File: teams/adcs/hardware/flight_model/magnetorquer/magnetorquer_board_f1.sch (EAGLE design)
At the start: 35 parts, among them U5 LTC3624

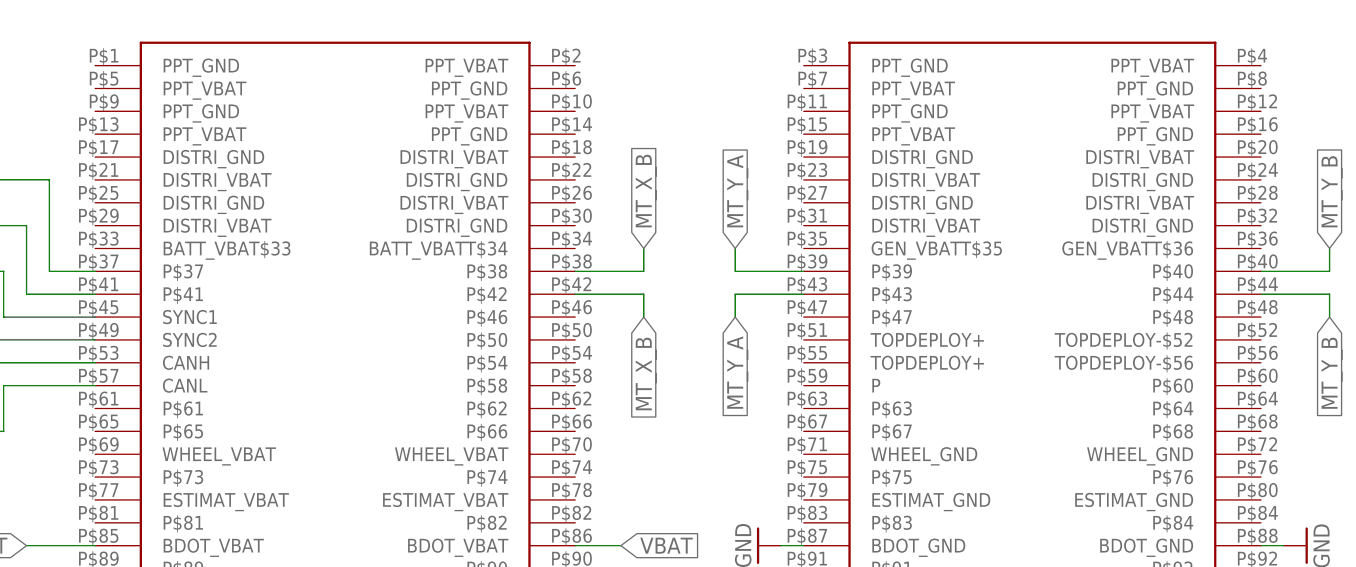
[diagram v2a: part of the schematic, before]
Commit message: ADCS/MT: Move buck converter and clean up stray traces
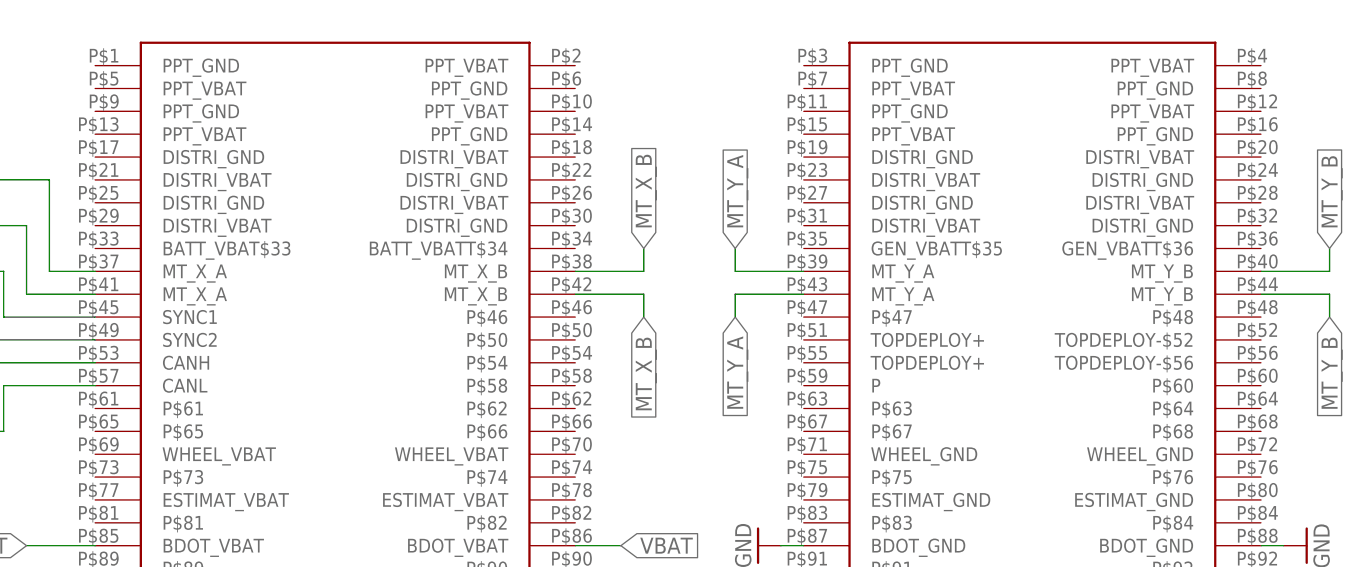
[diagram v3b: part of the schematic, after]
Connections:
- net MT_X_A: now also U$1.MT_X_A@1, U$1.MT_X_A@2; no longer U$1.P$37, U$1.P$41
- net MT_X_B: now also U$1.MT_X_B@1, U$1.MT_X_B@2; no longer U$1.P$38, U$1.P$42
- net MT_Y_A: now also U$1.MT_Y_A@1, U$1.MT_Y_A@2; no longer U$1.P$39, U$1.P$43
- net MT_Y_B: now also U$1.MT_Y_B@1, U$1.MT_Y_B@2; no longer U$1.P$40, U$1.P$44
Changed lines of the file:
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@@
 </segment>
 <segment>
-<pinref part="U$1" gate="G$1" pin="P$42"/>
+<pinref part="U$1" gate="G$1" pin="MT_X_B@2"/>
 <wire x1="30.48" y1="60.96" x2="38.1" y2="60.96" width="0.1524" layer="91"/>
 <wire x1="38.1" y1="60.96" x2="38.1" y2="58.42" width="0.1524" layer="91"/>
@@
 </segment>
 <segment>
-<pinref part="U$1" gate="G$1" pin="P$38"/>
+<pinref part="U$1" gate="G$1" pin="MT_X_B@1"/>
 <wire x1="30.48" y1="63.5" x2="38.1" y2="63.5" width="0.1524" layer="91"/>
 <wire x1="38.1" y1="63.5" x2="38.1" y2="66.04" width="0.1524" layer="91"/>
@@
 </segment>
 <segment>
-<pinref part="U$1" gate="G$1" pin="P$41"/>
+<pinref part="U$1" gate="G$1" pin="MT_X_A@2"/>
 <wire x1="-22.86" y1="60.96" x2="-30.48" y2="60.96" width="0.1524" layer="91"/>
 <wire x1="-30.48" y1="60.96" x2="-30.48" y2="68.58" width="0.1524" layer="91"/>
@@
 </segment>
 <segment>
-<pinref part="U$1" gate="G$1" pin="P$37"/>
+<pinref part="U$1" gate="G$1" pin="MT_X_A@1"/>
 <wire x1="-22.86" y1="63.5" x2="-27.94" y2="63.5" width="0.1524" layer="91"/>
 <wire x1="-27.94" y1="63.5" x2="-27.94" y2="73.66" width="0.1524" layer="91"/>
@@
 </segment>
 <segment>
-<pinref part="U$1" gate="G$1" pin="P$39"/>
+<pinref part="U$1" gate="G$1" pin="MT_Y_A@1"/>
 <wire x1="55.88" y1="63.5" x2="48.26" y2="63.5" width="0.1524" layer="91"/>
 <wire x1="48.26" y1="63.5" x2="48.26" y2="66.04" width="0.1524" layer="91"/>
@@
 </segment>
 <segment>
-<pinref part="U$1" gate="G$1" pin="P$43"/>
+<pinref part="U$1" gate="G$1" pin="MT_Y_A@2"/>
 <wire x1="55.88" y1="60.96" x2="48.26" y2="60.96" width="0.1524" layer="91"/>
 <wire x1="48.26" y1="60.96" x2="48.26" y2="58.42" width="0.1524" layer="91"/>
@@
 </segment>
 <segment>
-<pinref part="U$1" gate="G$1" pin="P$44"/>
+<pinref part="U$1" gate="G$1" pin="MT_Y_B@2"/>
 <wire x1="106.68" y1="60.96" x2="114.3" y2="60.96" width="0.1524" layer="91"/>
 <wire x1="114.3" y1="60.96" x2="114.3" y2="58.42" width="0.1524" layer="91"/>
@@
 </segment>
 <segment>
-<pinref part="U$1" gate="G$1" pin="P$40"/>
+<pinref part="U$1" gate="G$1" pin="MT_Y_B@1"/>
 <wire x1="106.68" y1="63.5" x2="114.3" y2="63.5" width="0.1524" layer="91"/>
 <wire x1="114.3" y1="63.5" x2="114.3" y2="66.04" width="0.1524" layer="91"/>
@@
 packages will not be understood (or retained) with this version.
 </note>
+<note version="8.4" severity="warning">
+Since Version 8.4, EAGLE supports properties for SPICE simulation.
+Probes in schematics and SPICE mapping objects found in parts and library devices
+will not be understood with this version. Update EAGLE to the latest version
+for full support of SPICE simulation.
+</note>
 </compatibility>

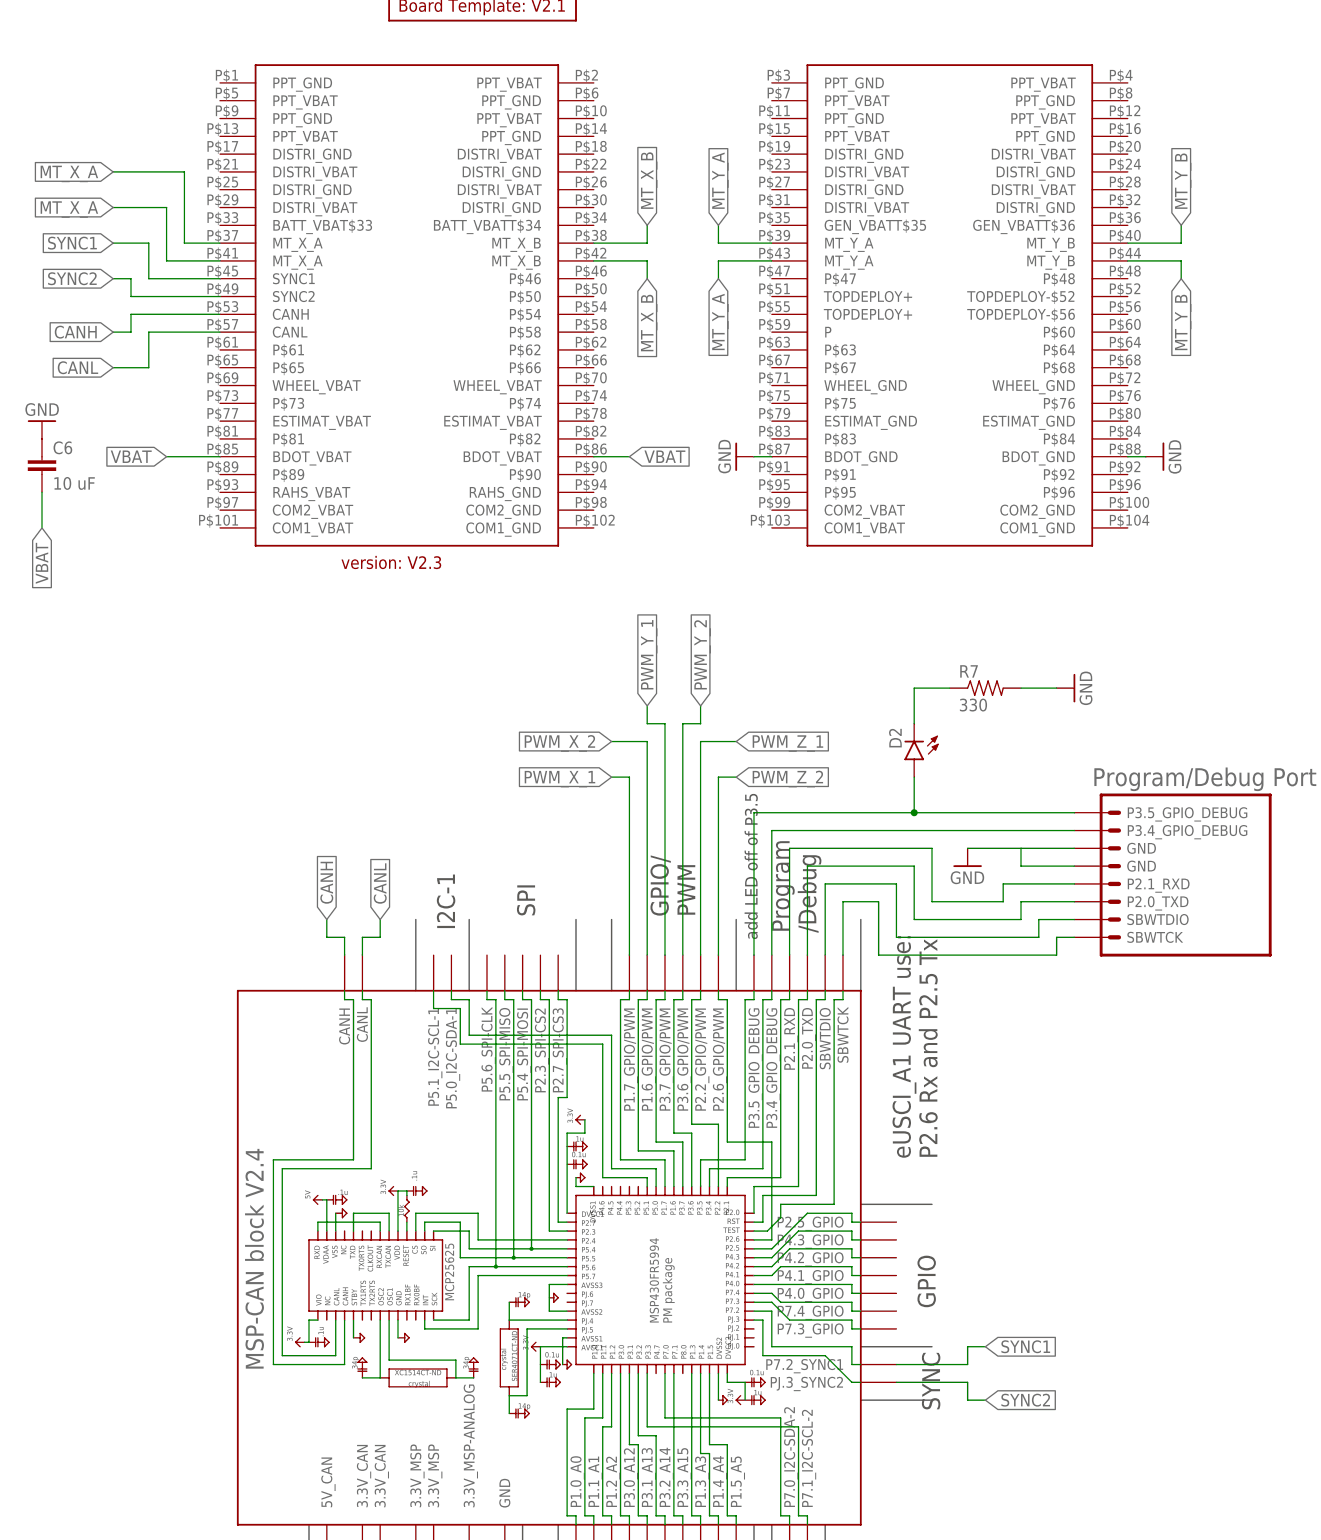
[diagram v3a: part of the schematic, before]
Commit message: ADCS/MT: Remove SYNC traces
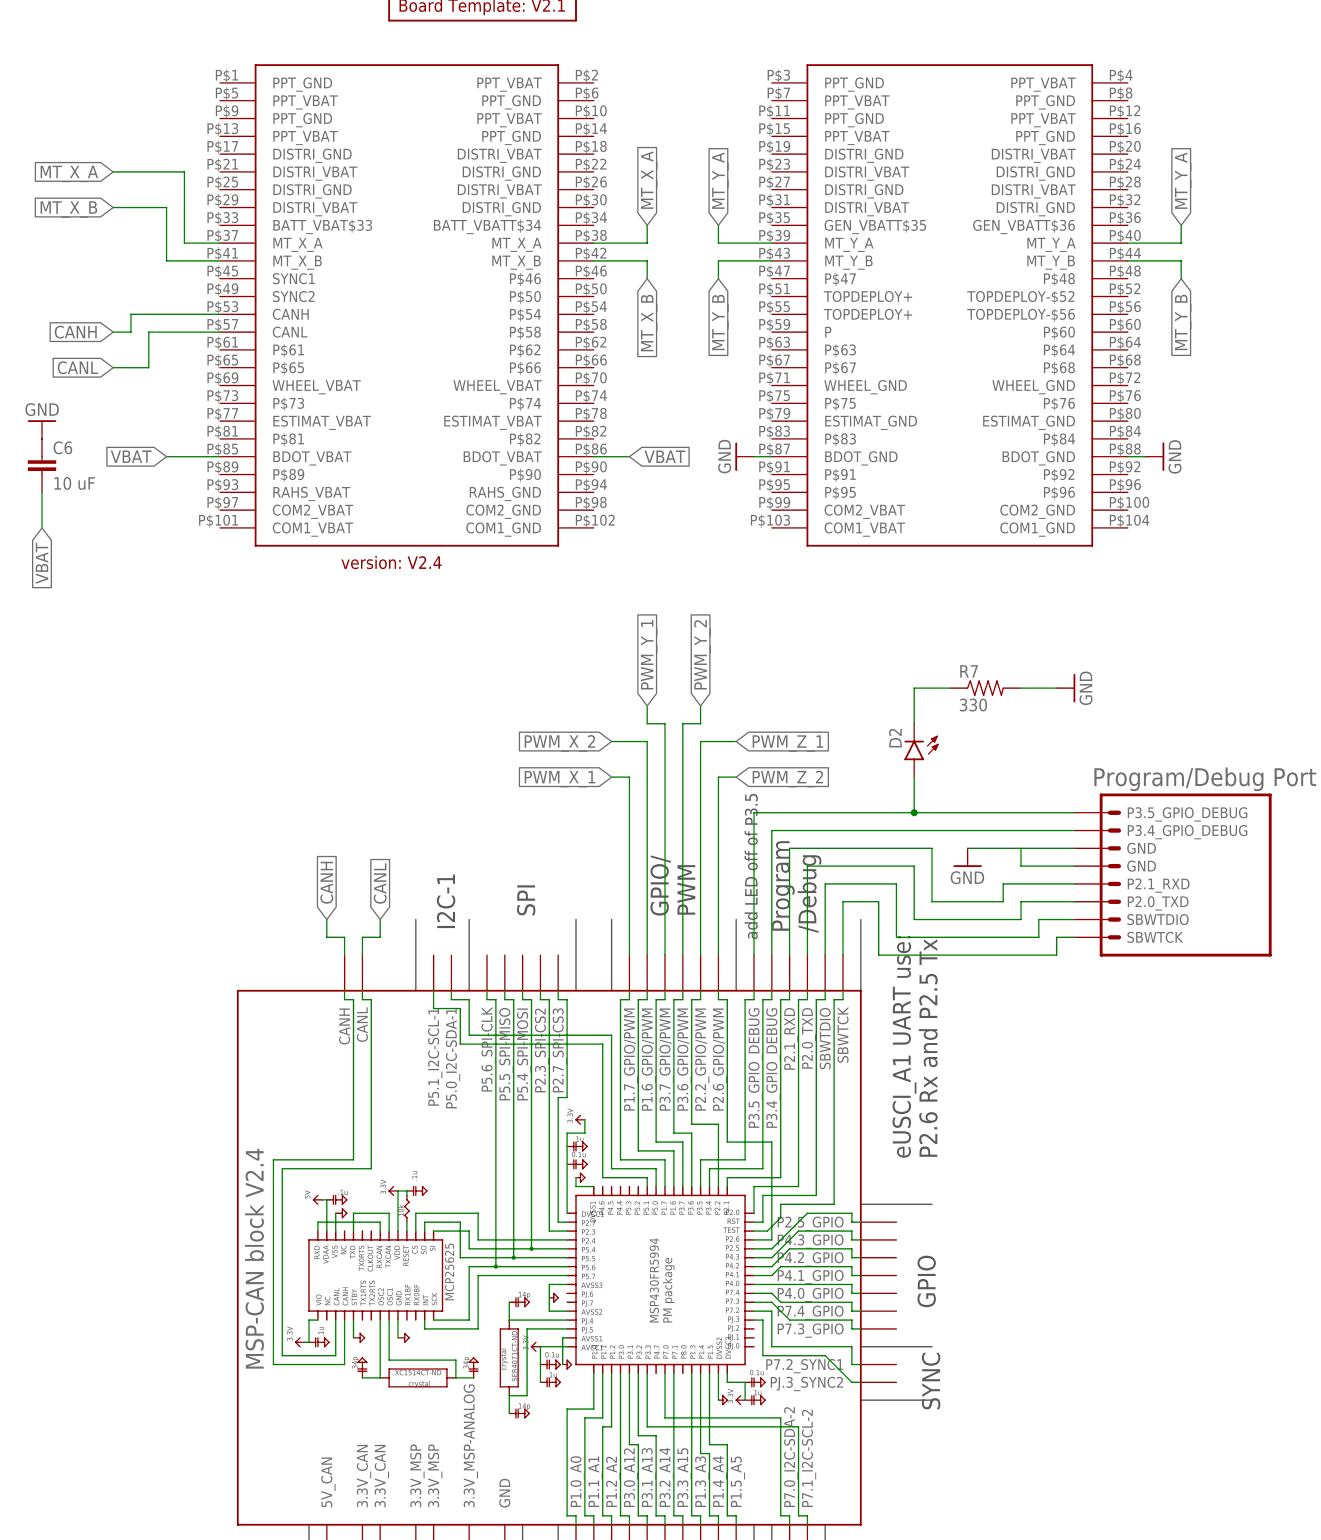
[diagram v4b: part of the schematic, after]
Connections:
- removed net SYNC1: U$1.SYNC1, U$7.P7.2_SYNC1
- removed net SYNC2: U$1.SYNC2, U$7.PJ.3_SYNC2
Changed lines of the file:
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@@
 <?xml version="1.0" encoding="utf-8"?>
 <!DOCTYPE eagle SYSTEM "eagle.dtd">
-<eagle version="8.7.1">
+<eagle version="9.0.0">
 <drawing>
 <settings>
-<setting alwaysvectorfont="no"/>
+<setting alwaysvectorfont="yes"/>
 <setting keepoldvectorfont="yes"/>
 <setting verticaltext="up"/>
@@
 </segment>
 <segment>
+<wire x1="-30.48" y1="60.96" x2="-30.48" y2="68.58" width="0.1524" layer="91"/>
+<wire x1="-30.48" y1="68.58" x2="-38.1" y2="68.58" width="0.1524" layer="91"/>
+<label x="-38.1" y="68.58" size="1.778" layer="95" rot="R180" xref="yes"/>
 <pinref part="U$1" gate="G$1" pin="MT_X_B@1"/>
-<wire x1="30.48" y1="63.5" x2="38.1" y2="63.5" width="0.1524" layer="91"/>
-<wire x1="38.1" y1="63.5" x2="38.1" y2="66.04" width="0.1524" layer="91"/>
-<label x="38.1" y="66.04" size="1.778" layer="95" rot="R90" xref="yes"/>
+<wire x1="-30.48" y1="60.96" x2="-22.86" y2="60.96" width="0.1524" layer="91"/>
 </segment>
 </net>
@@
 <wire x1="162.56" y1="68.58" x2="162.56" y2="88.9" width="0.1524" layer="91"/>
 <label x="162.56" y="88.9" size="1.778" layer="95" rot="R90" xref="yes"/>
-</segment>
-<segment>
-<pinref part="U$1" gate="G$1" pin="MT_X_A@2"/>
-<wire x1="-22.86" y1="60.96" x2="-30.48" y2="60.96" width="0.1524" layer="91"/>
-<wire x1="-30.48" y1="60.96" x2="-30.48" y2="68.58" width="0.1524" layer="91"/>
-<wire x1="-30.48" y1="68.58" x2="-38.1" y2="68.58" width="0.1524" layer="91"/>
-<label x="-38.1" y="68.58" size="1.778" layer="95" rot="R180" xref="yes"/>
 </segment>
 <segment>
@@
 <wire x1="-27.94" y1="73.66" x2="-38.1" y2="73.66" width="0.1524" layer="91"/>
 <label x="-38.1" y="73.66" size="1.778" layer="95" rot="R180" xref="yes"/>
+</segment>
+<segment>
+<wire x1="38.1" y1="63.5" x2="38.1" y2="66.04" width="0.1524" layer="91"/>
+<label x="38.1" y="66.04" size="1.778" layer="95" rot="R90" xref="yes"/>
+<pinref part="U$1" gate="G$1" pin="MT_X_A@2"/>
+<wire x1="38.1" y1="63.5" x2="30.48" y2="63.5" width="0.1524" layer="91"/>
 </segment>
 </net>
@@
 </segment>
 </net>
-<net name="SYNC2" class="0">
-<segment>
-<pinref part="U$1" gate="G$1" pin="SYNC2"/>
-<wire x1="-22.86" y1="55.88" x2="-35.56" y2="55.88" width="0.1524" layer="91"/>
-<wire x1="-35.56" y1="55.88" x2="-35.56" y2="58.42" width="0.1524" layer="91"/>
-<wire x1="-35.56" y1="58.42" x2="-38.1" y2="58.42" width="0.1524" layer="91"/>
-<label x="-38.1" y="58.42" size="1.778" layer="95" rot="R180" xref="yes"/>
-</segment>
-<segment>
-<pinref part="U$7" gate="G$1" pin="PJ.3_SYNC2"/>
-<wire x1="73.66" y1="-99.06" x2="83.82" y2="-99.06" width="0.1524" layer="91"/>
-<wire x1="83.82" y1="-99.06" x2="83.82" y2="-101.6" width="0.1524" layer="91"/>
-<wire x1="83.82" y1="-101.6" x2="86.36" y2="-101.6" width="0.1524" layer="91"/>
-<label x="86.36" y="-101.6" size="1.778" layer="95" xref="yes"/>
-</segment>
-</net>
-<net name="SYNC1" class="0">
-<segment>
-<pinref part="U$1" gate="G$1" pin="SYNC1"/>
-<wire x1="-22.86" y1="58.42" x2="-33.02" y2="58.42" width="0.1524" layer="91"/>
-<wire x1="-33.02" y1="58.42" x2="-33.02" y2="63.5" width="0.1524" layer="91"/>
-<wire x1="-33.02" y1="63.5" x2="-38.1" y2="63.5" width="0.1524" layer="91"/>
-<label x="-38.1" y="63.5" size="1.778" layer="95" rot="R180" xref="yes"/>
-</segment>
-<segment>
-<pinref part="U$7" gate="G$1" pin="P7.2_SYNC1"/>
-<wire x1="73.66" y1="-96.52" x2="83.82" y2="-96.52" width="0.1524" layer="91"/>
-<wire x1="83.82" y1="-96.52" x2="83.82" y2="-93.98" width="0.1524" layer="91"/>
-<wire x1="83.82" y1="-93.98" x2="86.36" y2="-93.98" width="0.1524" layer="91"/>
-<label x="86.36" y="-93.98" size="1.778" layer="95" xref="yes"/>
-</segment>
-</net>
 <net name="N$4" class="0">
 <segment>
@@
 </segment>
 <segment>
+<wire x1="114.3" y1="63.5" x2="114.3" y2="66.04" width="0.1524" layer="91"/>
+<label x="114.3" y="66.04" size="1.778" layer="95" rot="R90" xref="yes"/>
 <pinref part="U$1" gate="G$1" pin="MT_Y_A@2"/>
-<wire x1="55.88" y1="60.96" x2="48.26" y2="60.96" width="0.1524" layer="91"/>
-<wire x1="48.26" y1="60.96" x2="48.26" y2="58.42" width="0.1524" layer="91"/>
-<label x="48.26" y="58.42" size="1.778" layer="95" rot="R270" xref="yes"/>
+<wire x1="114.3" y1="63.5" x2="106.68" y2="63.5" width="0.1524" layer="91"/>
 </segment>
 </net>
@@
 </segment>
 <segment>
+<wire x1="48.26" y1="60.96" x2="48.26" y2="58.42" width="0.1524" layer="91"/>
+<label x="48.26" y="58.42" size="1.778" layer="95" rot="R270" xref="yes"/>
 <pinref part="U$1" gate="G$1" pin="MT_Y_B@1"/>
-<wire x1="106.68" y1="63.5" x2="114.3" y2="63.5" width="0.1524" layer="91"/>
-<wire x1="114.3" y1="63.5" x2="114.3" y2="66.04" width="0.1524" layer="91"/>
-<label x="114.3" y="66.04" size="1.778" layer="95" rot="R90" xref="yes"/>
-</segment>
-</net>
+<wire x1="48.26" y1="60.96" x2="55.88" y2="60.96" width="0.1524" layer="91"/>
+</segment>
+</net>
